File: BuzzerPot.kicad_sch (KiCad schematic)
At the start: 6 parts, among them J1 ConnM_01x03_Horizontal_2.54mm, Q2 AO3400_C4748804

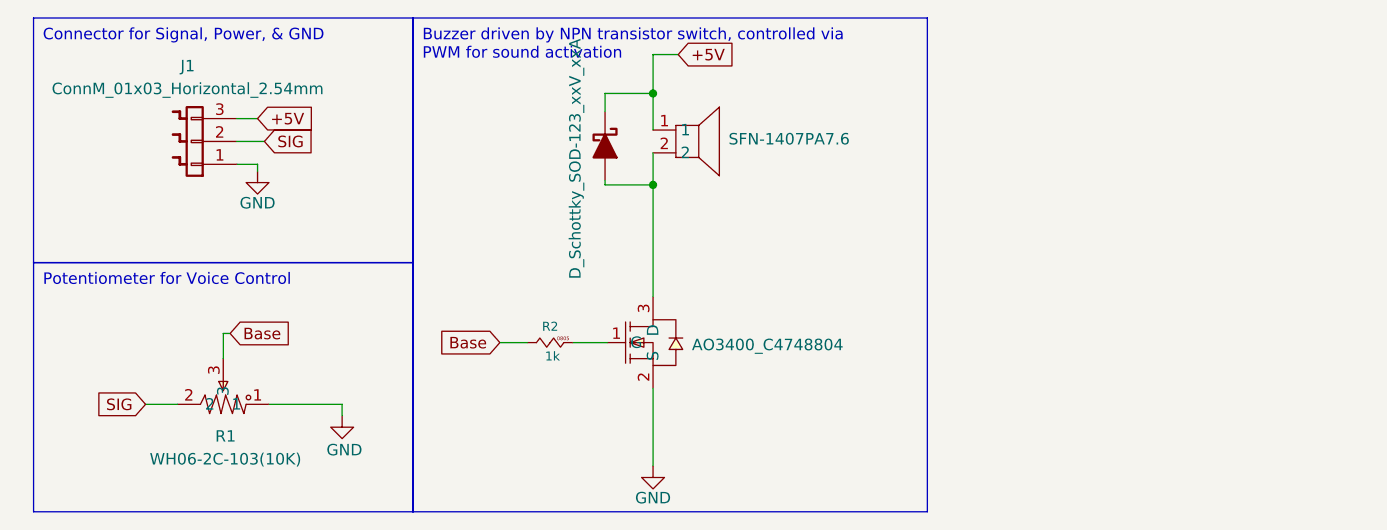
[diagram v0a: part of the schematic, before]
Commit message: Updated: Replaced Buzzer with Speaker
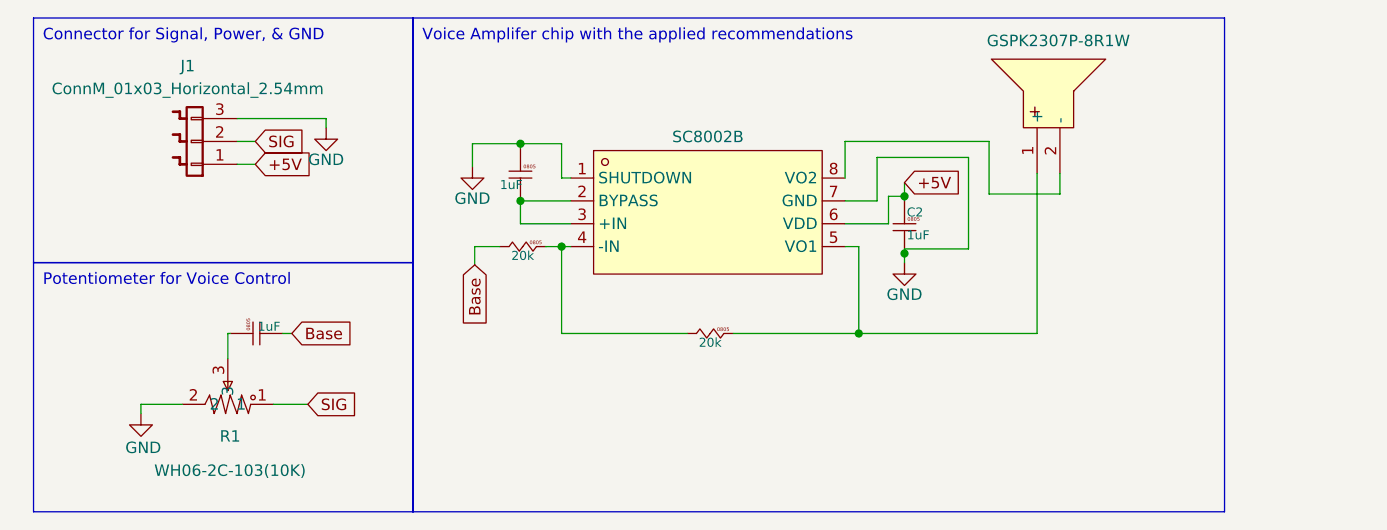
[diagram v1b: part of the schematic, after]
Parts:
- removed BUZZER2: SFN-1407PA7.6, easyeda2kicad:BUZ-TH_BD14.0-P7.60-D0.7, symbol easyeda2kicad:SFN-1407PA7.6
- removed D1: D_Schottky_SOD-123_xxV_xxA, Remal_KiCadLib:D_SOD-123, symbol Remal_KiCadLib:D_Schottky_SOD-123_xxV_xxA
- removed Q2: AO3400_C4748804, easyeda2kicad:SOT-23_L2.9-W1.3-P1.90-LS2.4-BR, symbol easyeda2kicad:AO3400_C4748804
- added C1, C2, C3: 1uF, Remal_KiCadLib:C_0805_2012m, symbol Remal_KiCadLib:C_0805_2012m
- added R3: 20k, Remal_KiCadLib:R_0805_2012m, symbol Remal_KiCadLib:R_0805_2012m
- added SPK1: GSPK2307P-8R1W, easyeda2kicad:SPK-TH_BD23.0-P10.00-D0.8-L-RD, symbol easyeda2kicad:GSPK2307P-8R1W
- added U1: SC8002B, easyeda2kicad:SOP-8_L4.9-W3.9-P1.27-LS6.0-BL, symbol easyeda2kicad:SC8002B
- R2: value 1k -> 20k
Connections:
- net +5V: now also J1.1 (Pin_1), C2.1, U1.6 (VDD); no longer J1.3 (Pin_3)
- net Base: now also C3.2; no longer R1.3
- net GND: now also J1.3 (Pin_3), R1.2, C1.1, C2.2, U1.1 (SHUTDOWN), U1.7 (GND); no longer J1.1 (Pin_1), R1.1
- net SIG: now also R1.1; no longer R1.2
- net at R2.2: now also R3.1, U1.4 (-IN)
- new net: R3.2, SPK1.1 (+), U1.5 (VO1)
- new net: SPK1.2 (-), U1.8 (VO2)
- new net: C1.2, U1.2 (BYPASS), U1.3 (+IN)
- new net: C3.1, R1.3

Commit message: Updated Version 2
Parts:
- removed C3: 1uF, Remal_KiCadLib:C_0805_2012m, symbol Remal_KiCadLib:C_0805_2012m
- removed R1: WH06-2C-103(10K), easyeda2kicad:RES-ADJ-TH_WH06-2C-103, symbol easyeda2kicad:WH06-2C-103(10K)
- removed R2: 20k, Remal_KiCadLib:R_0805_2012m, symbol Remal_KiCadLib:R_0805_2012m
- added C3: 1uF, Remal_KiCadLib:C_0402_1005m, symbol Remal_KiCadLib:C_0402_1005m
- added H1: MountingHole_3.2mm_M3_NoConn, Remal_KiCadLib:MountingHole_3.2mm_M3_NoConn, symbol Remal_KiCadLib:MountingHole_3.2mm_M3_NoConn
- added R2: 20k, Remal_KiCadLib:R_0402_1005m, symbol Remal_KiCadLib:R_0402_1005m
- added R4: WH06-2C-103(10K), easyeda2kicad:RES-ADJ-TH_WH06-2C-103, symbol easyeda2kicad:WH06-2C-103(10K)
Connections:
- net Base: now also C3.2, R2.1
- net GND: now also R4.2
- net SIG: now also R4.1
- net at R3.1, U1.4 (-IN): now also R2.2
- new net: C3.1, R4.3

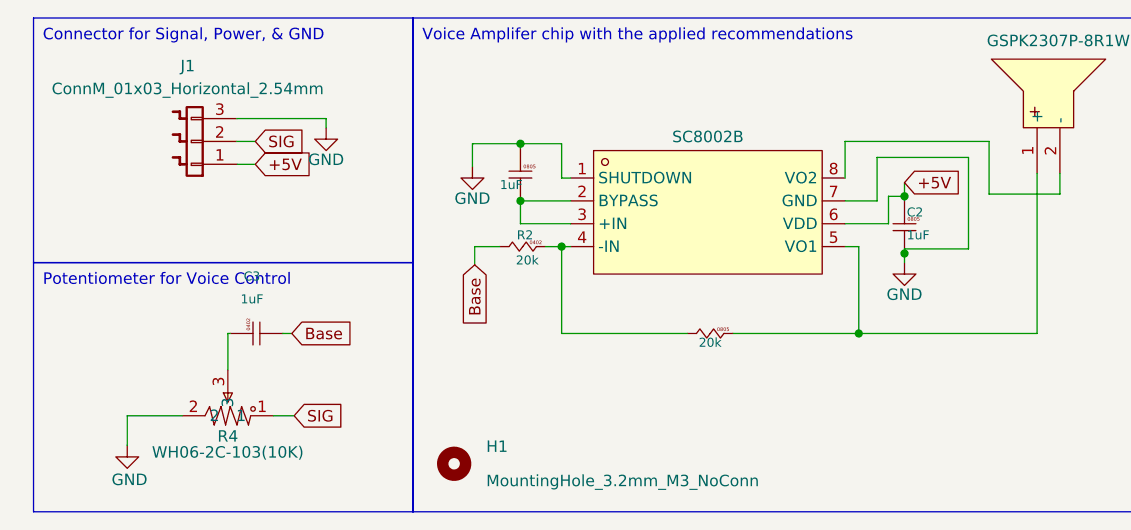
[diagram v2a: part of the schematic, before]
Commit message: Last Changes: Added Logo and Name
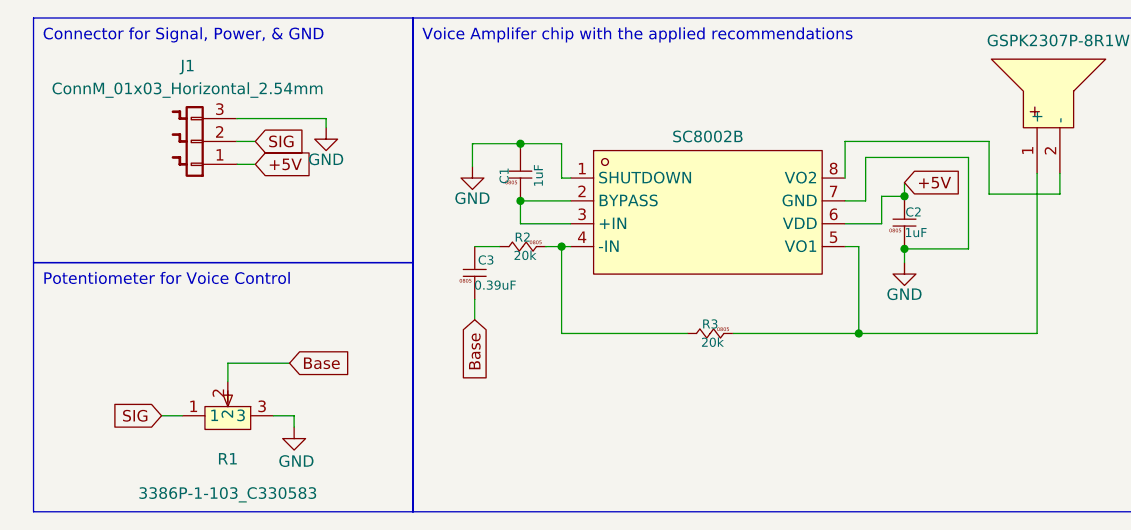
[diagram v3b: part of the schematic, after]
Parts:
- removed C3: 1uF, Remal_KiCadLib:C_0402_1005m, symbol Remal_KiCadLib:C_0402_1005m
- removed H1: MountingHole_3.2mm_M3_NoConn, Remal_KiCadLib:MountingHole_3.2mm_M3_NoConn, symbol Remal_KiCadLib:MountingHole_3.2mm_M3_NoConn
- removed R2: 20k, Remal_KiCadLib:R_0402_1005m, symbol Remal_KiCadLib:R_0402_1005m
- removed R4: WH06-2C-103(10K), easyeda2kicad:RES-ADJ-TH_WH06-2C-103, symbol easyeda2kicad:WH06-2C-103(10K)
- added C3: 0.39uF, Remal_KiCadLib:C_0805_2012m, symbol Remal_KiCadLib:C_0805_2012m
- added R1: 3386P-1-103_C330583, easyeda2kicad:RES-ADJ-TH_3P-L9.5-W9.5-P2.50-L_3386P, symbol easyeda2kicad:3386P-1-103_C330583
- added R2: 20k, Remal_KiCadLib:R_0805_2012m, symbol Remal_KiCadLib:R_0805_2012m
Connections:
- net +5V: now also C2.2; no longer C2.1
- net Base: now also C3.1, R1.2
- net GND: now also C1.2, C2.1, R1.3; no longer C1.1, C2.2
- net SIG: now also R1.1
- net at R3.1, U1.4 (-IN): now also R2.2
- net at U1.2 (BYPASS), U1.3 (+IN): now also C1.1; no longer C1.2
- new net: C3.2, R2.1

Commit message: Updated: Remal Golden Standard Recheck
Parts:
- added R4: 47k, Remal_KiCadLib:R_0805_2012m, symbol Remal_KiCadLib:R_0805_2012m
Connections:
- net +5V: now also R4.2
- net GND: now also R4.1
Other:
- moved on the sheet: C1, C2, C3, R2, R3

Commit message: Last Update: Inserted two Mounting Holes M2
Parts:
- added H1, H2: MountingHole_2.2mm_M2_NoConn, Remal_KiCadLib:MountingHole_2.2mm_M2_NoConn, symbol Remal_KiCadLib:MountingHole_2.2mm_M2_NoConn
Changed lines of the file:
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@@
+	)
+	(symbol
+		(lib_id "Remal_KiCadLib:MountingHole_2.2mm_M2_NoConn")
+		(at 35.052 80.01 0)
+		(unit 1)
+		(exclude_from_sim no)
+		(in_bom yes)
+		(on_board yes)
+		(dnp no)
+		(property "Reference" "H2"
+			(at 37.084 79.756 0)
+			(effects
+				(font
+					(size 1.27 1.27)
+				)
+				(justify left)
+			)
+		)
+		(property "Value" "MountingHole_2.2mm_M2_NoConn"
+			(at 37.084 81.534 0)
+			(effects
+				(font
+					(size 1.27 1.27)
+				)
+				(justify left)
+			)
+		)
+		(property "Footprint" "Remal_KiCadLib:MountingHole_2.2mm_M2_NoConn"
+			(at 35.306 83.312 0)
+			(effects
+				(font
+					(size 1.27 1.27)
+				)
+				(hide yes)
+			)
+		)
+		(property "Datasheet" "~"
+			(at 35.306 84.836 0)
+			(effects
+				(font
+					(size 1.27 1.27)
+				)
+				(hide yes)
+			)
+		)
+		(property "Description" "Mounting Hole 2.2mm M2 without connection"
+			(at 35.306 83.312 0)
+			(effects
+				(font
+					(size 1.27 1.27)
+				)
+				(hide yes)
+			)
+		)
+		(instances
+			(project ""
+				(path "/bf042a33-1684-4ee5-aab2-ce4b698ddb84"
+					(reference "H2")
+					(unit 1)
+				)
+			)
+		)
 	)
 	(symbol
@@
 					(unit 1)
 				)
+			)
+		)
+	)
+	(symbol
+		(lib_id "Remal_KiCadLib:MountingHole_2.2mm_M2_NoConn")
+		(at 35.306 73.66 0)
+		(unit 1)
+		(exclude_from_sim no)
+		(in_bom yes)
+		(on_board yes)
+		(dnp no)
+		(property "Reference" "H1"
+			(at 37.084 73.152 0)
+			(effects
+				(font
+					(size 1.27 1.27)
+				)
+				(justify left)
+			)
+		)
+		(property "Value" "MountingHole_2.2mm_M2_NoConn"
+			(at 37.084 75.184 0)
+			(effects
+				(font
+					(size 1.27 1.27)
+				)
+				(justify left)
+			)
+		)
+		(property "Footprint" "Remal_KiCadLib:MountingHole_2.2mm_M2_NoConn"
+			(at 35.56 76.962 0)
+			(effects
+				(font
+					(size 1.27 1.27)
+				)
+				(hide yes)
+			)
+		)
+		(property "Datasheet" "~"
+			(at 35.56 78.486 0)
+			(effects
+				(font
+					(size 1.27 1.27)
+				)
+				(hide yes)
+			)
+		)
+		(property "Description" "Mounting Hole 2.2mm M2 without connection"
+			(at 35.56 76.962 0)
+			(effects
+				(font
+					(size 1.27 1.27)
+				)
+				(hide yes)
+			)
+		)
+		(instances
+			(project ""
+				(path "/bf042a33-1684-4ee5-aab2-ce4b698ddb84"
+					(reference "H1")
+					(unit 1)
+				)
